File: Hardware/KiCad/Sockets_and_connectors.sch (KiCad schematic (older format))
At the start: 28 parts, among them J19 POWER_JACKPTH, Q4 FDN340P, Q5 FDN340P, SW1 SW_SPDT, U2 LM358, U3 AMS1117-3.3, U8 MP2307SO

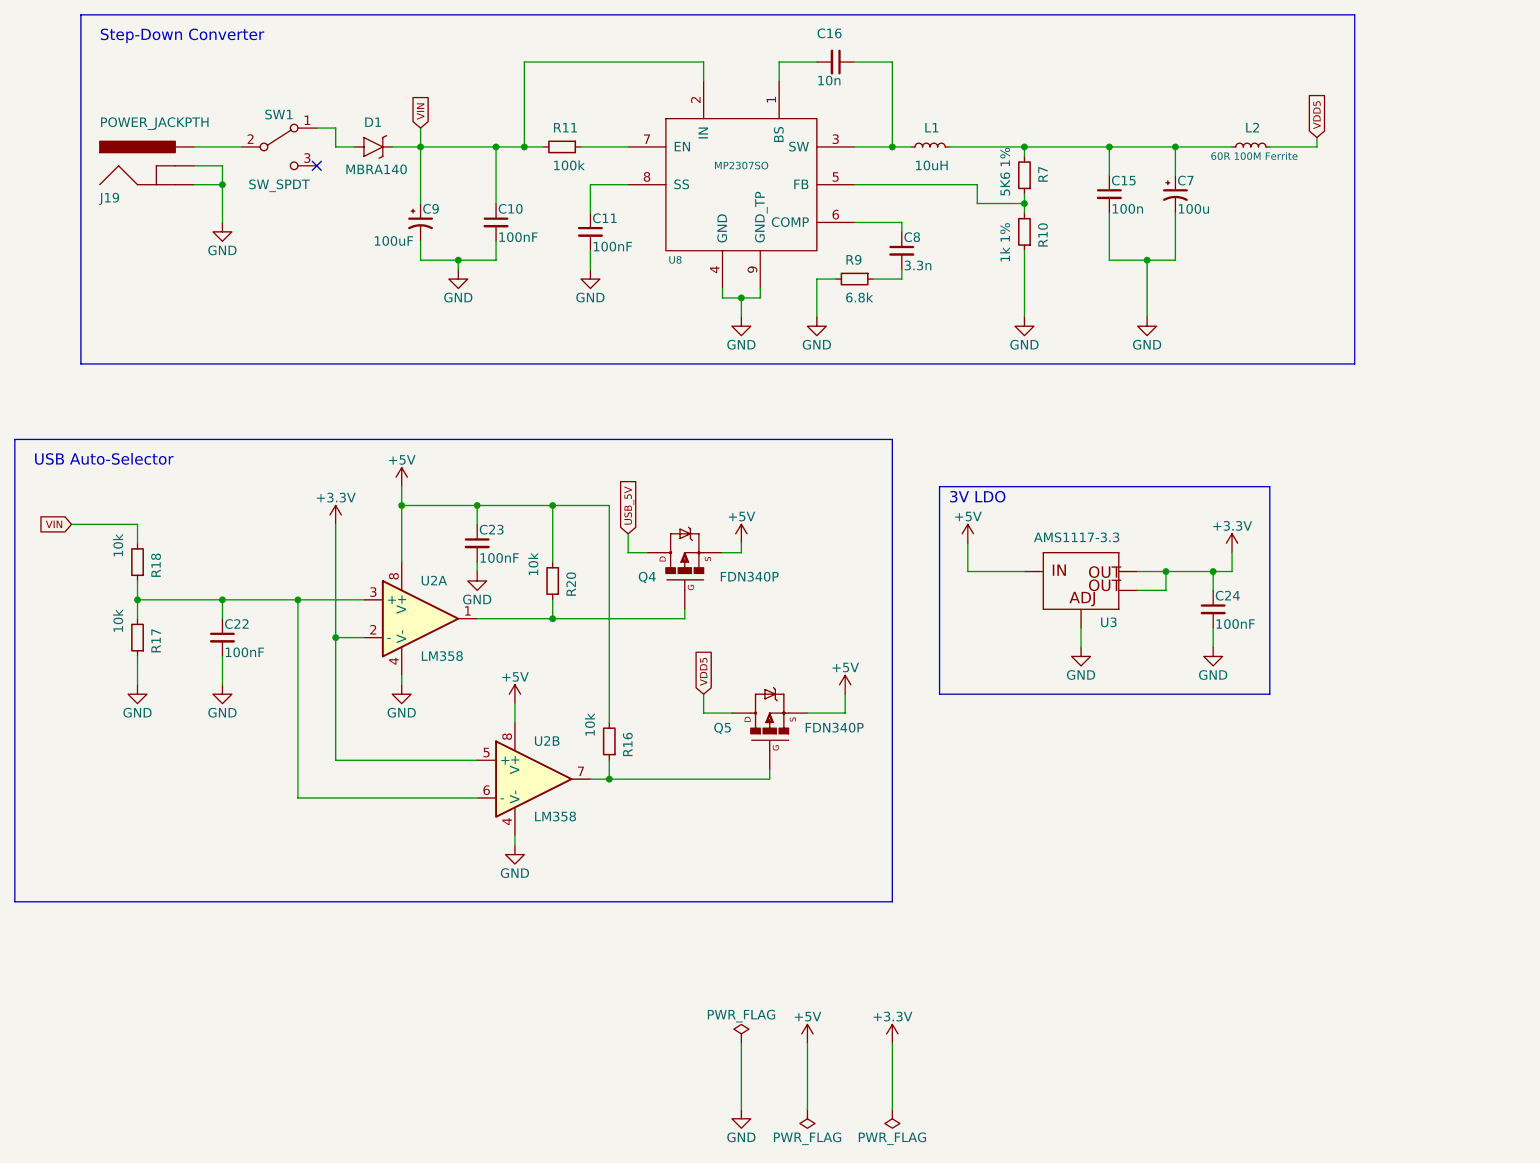
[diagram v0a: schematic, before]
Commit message: Cambiando el árbol de carpetas
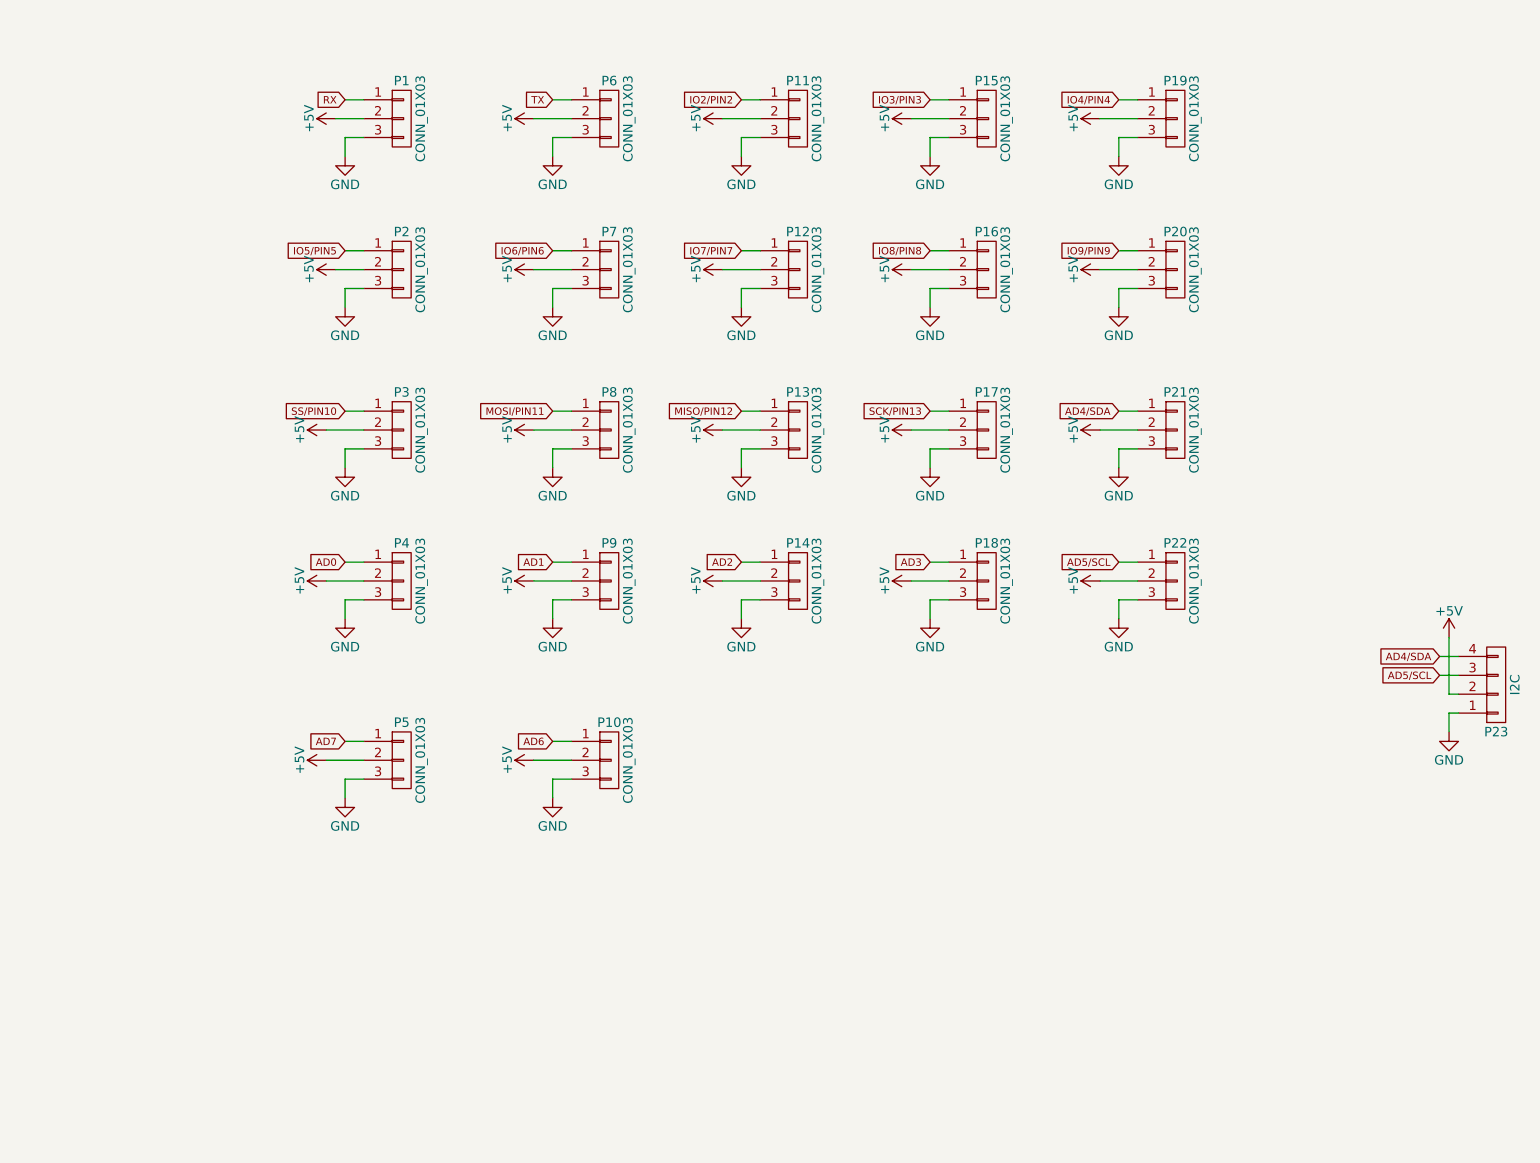
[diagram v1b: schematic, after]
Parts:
- removed C10, C11, C22, C23, C24: 100nF, Capacitors_SMD:C_0805, symbol C_Small
- removed C15: 100n, Capacitors_SMD:C_0805, symbol C_Small
- removed C16: 10n, Capacitors_SMD:C_0805, symbol C_Small
- removed C7: 100u, Capacitors_SMD:CP_Elec_6.3x5.3, symbol CP1_Small
- removed C8: 3.3n, Capacitors_SMD:C_0805, symbol C_Small
- removed C9: 100uF, Capacitors_SMD:CP_Elec_6.3x5.3, symbol CP1_Small
- removed D1: MBRA140, Diodes_SMD:D_SMA, symbol MBRA140
- removed J19: POWER_JACKPTH, Connectors:JACK_ALIM, symbol POWER_JACKPTH
- removed L1: 10uH, Inductors_SMD:L_Wuerth_WE-PD2-Typ-L, symbol L_Small
- removed L2: 60R 100M Ferrite, Inductors_SMD:L_0805, symbol L_Small
- removed Q4, Q5: FDN340P, TO_SOT_Packages_SMD:SOT-23, symbol MOSFET-PCHANNEL
- removed R10: 1k 1%, Resistors_SMD:R_0805, symbol R_Small
- removed R11: 100k, Resistors_SMD:R_0805, symbol R_Small
- removed R16, R17, R18, R20: 10k, Resistors_SMD:R_0805, symbol R_Small
- removed R7: 5K6 1%, Resistors_SMD:R_0805, symbol R_Small
- removed R9: 6.8k, Resistors_SMD:R_0805, symbol R_Small
- removed SW1: SW_SPDT, Buttons_Switches_SMD:SW_SPDT_PCM12, symbol SW_SPDT
- removed U2: LM358, Housings_SOIC:SOIC-8_3.9x4.9mm_Pitch1.27mm, symbol LM358
- removed U3: AMS1117-3.3, TO_SOT_Packages_SMD:SOT-223, symbol V_REG_LM1117SOT223
- removed U8: MP2307SO, Housings_SOIC:HTSOP-8-1EP_3.9x4.9mm_Pitch1.27mm_ThermalVias_LargeCopper, symbol MP2307SO
- added P1, P10, P11, P12, P13, P14, P15, P16, P17, P18, P19, P2, P20, P21, P22, P3, P4, P5, P6, P7, P8, P9: CONN_01X03, lib_sch:Pin_Header_Straight_1x03_Pitch2.54mm, symbol CONN_01X03
- added P23: I2C, lib_sch:JST_PH_S4B-PH-K_04x2.00mm_Angled, symbol CONN_01X04
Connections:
- net +5V: now also P1.2 (P2), P10.2 (P2), P11.2 (P2), P12.2 (P2), P13.2 (P2), P14.2 (P2), P15.2 (P2), P16.2 (P2), P17.2 (P2), P18.2 (P2), P19.2 (P2), P2.2 (P2), P20.2 (P2), P21.2 (P2), P22.2 (P2), P23.2 (P2), P3.2 (P2), P4.2 (P2), P5.2 (P2), P6.2 (P2), P7.2 (P2), P8.2 (P2), P9.2 (P2)
- net GND: now also P1.3 (P3), P10.3 (P3), P11.3 (P3), P12.3 (P3), P13.3 (P3), P14.3 (P3), P15.3 (P3), P16.3 (P3), P17.3 (P3), P18.3 (P3), P19.3 (P3), P2.3 (P3), P20.3 (P3), P21.3 (P3), P22.3 (P3), P23.1 (P1), P3.3 (P3), P4.3 (P3), P5.3 (P3), P6.3 (P3), P7.3 (P3), P8.3 (P3), P9.3 (P3)
- new net AD0: P4.1 (P1)
- new net AD1: P9.1 (P1)
- new net AD2: P14.1 (P1)
- new net AD3: P18.1 (P1)
- new net AD4/SDA: P21.1 (P1), P23.4 (P4)
- new net AD5/SCL: P22.1 (P1), P23.3 (P3)
- new net AD6: P10.1 (P1)
- new net AD7: P5.1 (P1)
- new net IO2/PIN2: P11.1 (P1)
- new net IO3/PIN3: P15.1 (P1)
- new net IO4/PIN4: P19.1 (P1)
- new net IO5/PIN5: P2.1 (P1)
- new net IO6/PIN6: P7.1 (P1)
- new net IO7/PIN7: P12.1 (P1)
- new net IO8/PIN8: P16.1 (P1)
- new net IO9/PIN9: P20.1 (P1)
- new net MISO/PIN12: P13.1 (P1)
- new net MOSI/PIN11: P8.1 (P1)
- new net RX: P1.1 (P1)
- new net SCK/PIN13: P17.1 (P1)
- new net SS/PIN10: P3.1 (P1)
- new net TX: P6.1 (P1)
- no-connect marks 1 -> 0
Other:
- note removed: "3V LDO"
- note removed: "Step-Down Converter"
- note removed: "USB Auto-Selector"
